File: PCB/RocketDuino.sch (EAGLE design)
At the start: 44 parts, among them J1 FTDI, Y1 16MHZ

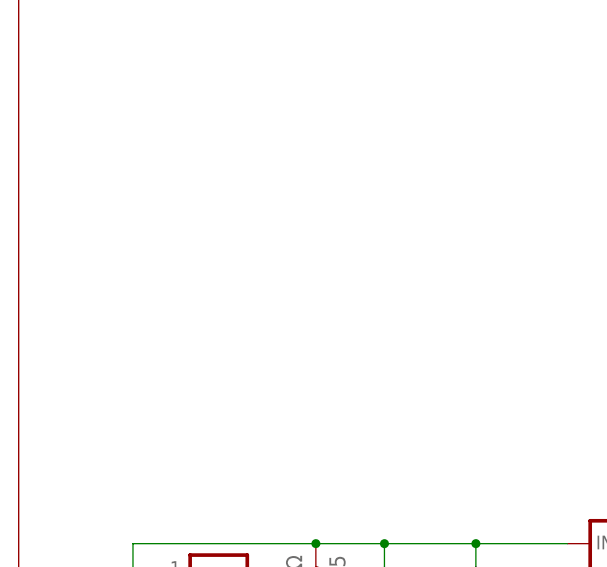
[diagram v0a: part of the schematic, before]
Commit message: Silkscreen changes
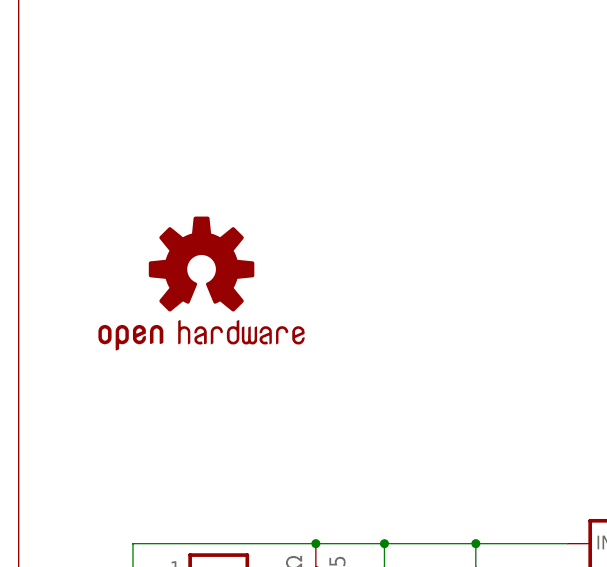
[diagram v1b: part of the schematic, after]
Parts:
- added LOGO2: OSHW-LOGOM, SparkFun-Aesthetics:OSHW-LOGOM
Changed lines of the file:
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@@
 <part name="SUPPLY7" library="SparkFun-Aesthetics" deviceset="5V" device=""/>
 <part name="GND10" library="SparkFun-Aesthetics" deviceset="GND" device=""/>
+<part name="LOGO2" library="SparkFun-Aesthetics" deviceset="OSHW-LOGO" device="M" value="OSHW-LOGOM"/>
 </parts>
 <sheets>
@@
 <instance part="SUPPLY7" gate="G$1" x="269.24" y="185.42" rot="R180"/>
 <instance part="GND10" gate="1" x="269.24" y="193.04" rot="R180"/>
+<instance part="LOGO2" gate="G$1" x="15.24" y="71.12"/>
 </instances>
 <busses>
